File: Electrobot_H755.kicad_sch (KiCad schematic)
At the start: 108 parts, among them J1 Conn_XT30M, J10 Conn_01x04, J11 Conn_01x04, J12 Conn_01x04, J13 Conn_01x04, J14 Conn_01x04, J15 Conn_01x03, J16 Conn_01x03, J17 Conn_01x04, J18 Conn_01x03, J19 Conn_01x03, J2 Conn_01x04, J20 Conn_01x03, J21 Conn_01x03, J22 Conn_01x04, J23 Conn_01x03, J24 Conn_01x03, J25 Conn_01x03, J26 Conn_01x03, J27 Conn_01x02, J28 Conn_01x02, J29 Conn_01x02, J3 Conn_01x04, J30 Conn_01x02, J31 Conn_01x03, J32 Conn_01x03, J33 Conn_01x06, J34 Conn_01x06, J35 Conn_01x04, J36 Conn_01x02, J37 Conn_01x04, J4 Conn_01x04, J5 Conn_01x04, J6 Conn_01x04, J7 Conn_01x04, J8 Conn_01x04, J9 Conn_01x04, U2 TSR_2-2450, U3 TSR_2-2465, U4 TSR_2-2465

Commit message: Ajout des références pour les supports sécables femelle 2.54
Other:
- note added: "Support 2.54 sécable femelle à souder RS: 766-6666 / 488-1724 / 827-7659"
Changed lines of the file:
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@@
+		)
+	)
+	(text "Support 2.54 sécable femelle à souder\nRS: 766-6666 / 488-1724 / 827-7659"
+		(exclude_from_sim no)
+		(at 104.902 193.548 0)
+		(effects
+			(font
+				(size 1.016 1.016)
+			)
+			(justify left)
 		)
 	)

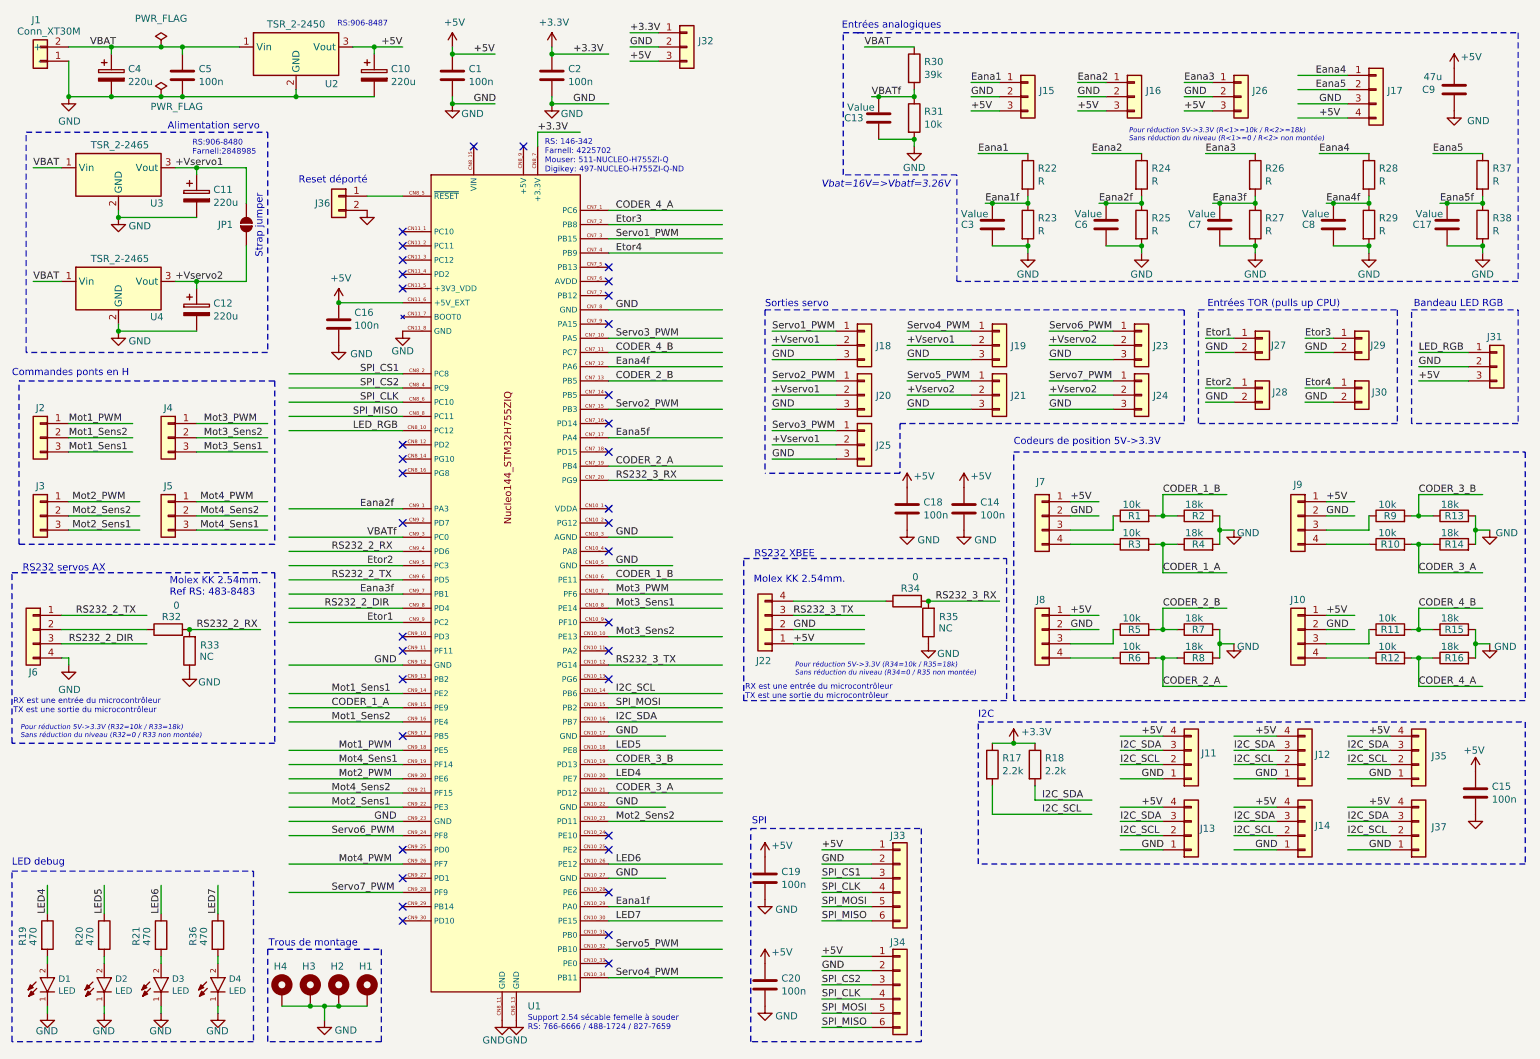
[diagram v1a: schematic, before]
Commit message: Ajout des références et valeurs manquantes sur le schéma
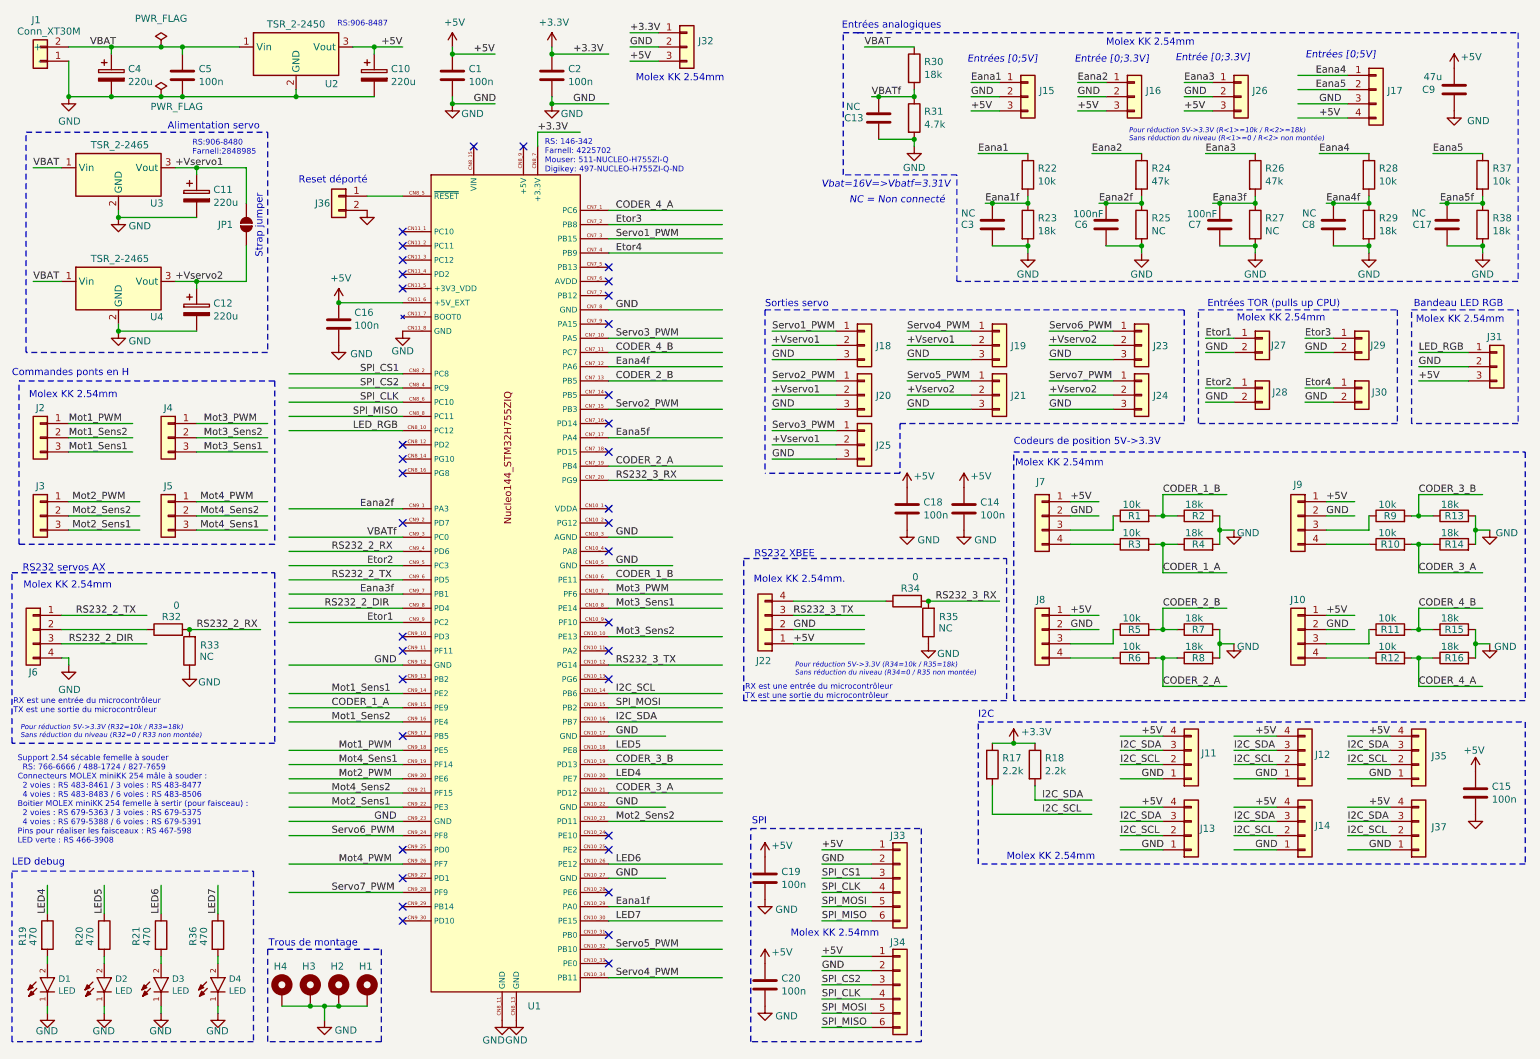
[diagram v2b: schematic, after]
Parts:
- C13, C17, C3, C8: value Value -> NC
- C6, C7: value Value -> 100nF
- R22, R28, R37: value R -> 10k
- R23, R29, R38: value R -> 18k
- R24, R26: value R -> 47k
- R25, R27: value R -> NC
- R30: value 39k -> 18k
- R31: value 10k -> 4.7k
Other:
- note added: "Entrée [0;3.3V]"
- note added: "Entrées [0;5V]"
- note added: "Molex KK 2.54mm"
- note added: "NC = Non connecté"
- note added: "Support 2.54 sécable femelle à souder RS: 766-6666 / 488-1724 / 827-7659 Connecteurs MOLEX miniKK 254 mâle à souder : 2 voies : RS 483-8461 / 3 voies : RS 483-8477 4 voies : RS 483-8483 / 6 voies : RS 483-8506 Boitier MOLEX miniKK 254 femelle à sertir (pour faisceau) : 2 voies : RS 679-5363 / 3 voies : RS 679-5375 4 voies : RS 679-5388 / 6 voies : RS 679-5391 Pins pour réaliser les faisceaux : RS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"
- note added: "Vbat=16V=>Vbatf=3.31V"
- note removed: "Molex KK 2.54mm. Ref RS: 483-8483"
- note removed: "Support 2.54 sécable femelle à souder RS: 766-6666 / 488-1724 / 827-7659"
- note removed: "Vbat=16V=>Vbatf=3.26V"
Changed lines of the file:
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@@
 		)
 	)
+	(text "Entrée [0;3.3V]"
+		(exclude_from_sim no)
+		(at 227.33 21.082 0)
+		(effects
+			(font
+				(size 1.27 1.27)
+				(italic yes)
+			)
+		)
+	)
 	(text "Sorties servo"
 		(exclude_from_sim no)
@@
 		)
 	)
-	(text "Vbat=16V=>Vbatf=3.26V"
+	(text "Molex KK 2.54mm"
+		(exclude_from_sim no)
+		(at 192.024 94.234 0)
+		(effects
+			(font
+				(size 1.27 1.27)
+			)
+			(justify left bottom)
+		)
+	)
+	(text "Molex KK 2.54mm"
+		(exclude_from_sim no)
+		(at 190.5 164.592 0)
+		(effects
+			(font
+				(size 1.27 1.27)
+			)
+			(justify left bottom)
+		)
+	)
+	(text "Entrées [0;5V]"
+		(exclude_from_sim no)
+		(at 189.738 21.336 0)
+		(effects
+			(font
+				(size 1.27 1.27)
+				(italic yes)
+			)
+		)
+	)
+	(text "Molex KK 2.54mm"
+		(exclude_from_sim no)
+		(at 124.206 25.4 0)
+		(effects
+			(font
+				(size 1.27 1.27)
+			)
+			(justify left bottom)
+		)
+	)
+	(text "Vbat=16V=>Vbatf=3.31V"
 		(exclude_from_sim no)
 		(at 168.91 43.688 0)
@@
 		)
 	)
+	(text "Molex KK 2.54mm"
+		(exclude_from_sim no)
+		(at 263.652 68.58 0)
+		(effects
+			(font
+				(size 1.27 1.27)
+			)
+			(justify left bottom)
+		)
+	)
 	(text "Commandes ponts en H"
 		(exclude_from_sim no)
@@
 		)
 	)
+	(text "Entrées [0;5V]"
+		(exclude_from_sim no)
+		(at 250.19 20.574 0)
+		(effects
+			(font
+				(size 1.27 1.27)
+				(italic yes)
+			)
+		)
+	)
 	(text "RS232 XBEE"
 		(exclude_from_sim no)
@@
 		)
 	)
-	(text "Molex KK 2.54mm.\nRef RS: 483-8483"
+	(text "Molex KK 2.54mm"
 		(exclude_from_sim no)
-		(at 40.894 117.348 0)
+		(at 14.732 116.078 0)
 		(effects
 			(font
@@
 		)
 	)
+	(text "NC = Non connecté"
+		(exclude_from_sim no)
+		(at 170.942 46.482 0)
+		(effects
+			(font
+				(size 1.27 1.27)
+				(italic yes)
+			)
+		)
+	)
 	(text "Pour réduction 5V->3.3V (R32=10k / R33=18k)\nSans réduction du niveau (R32=0 / R33 non montée)\n\n"
 		(exclude_from_sim no)
@@
 		)
 	)
+	(text "Entrée [0;3.3V]"
+		(exclude_from_sim no)
+		(at 209.296 21.336 0)
+		(effects
+			(font
+				(size 1.27 1.27)
+				(italic yes)
+			)
+		)
+	)
 	(text "Entrées TOR (pulls up CPU)"
 		(exclude_from_sim no)
@@
 		)
 	)
-	(text "Support 2.54 sécable femelle à souder\nRS: 766-6666 / 488-1724 / 827-7659"
+	(text "Molex KK 2.54mm"
 		(exclude_from_sim no)
-		(at 104.902 193.548 0)
+		(at 231.648 68.326 0)
 		(effects
 			(font
-				(size 1.016 1.016)
+				(size 1.27 1.27)
 			)
-			(justify left)
+			(justify left bottom)
 		)
 	)
@@
 		)
 	)
+	(text "Molex KK 2.54mm"
+		(exclude_from_sim no)
+		(at 151.892 178.308 0)
+		(effects
+			(font
+				(size 1.27 1.27)
+			)
+			(justify left bottom)
+		)
+	)
 	(text "RS232 servos AX"
 		(exclude_from_sim no)
@@
 		)
 	)
+	(text "Molex KK 2.54mm"
+		(exclude_from_sim no)
+		(at 208.28 19.05 0)
+		(effects
+			(font
+				(size 1.27 1.27)
+			)
+			(justify left bottom)
+		)
+	)
 	(text "I2C"
 		(exclude_from_sim no)
@@
 		)
 	)
+	(text "Molex KK 2.54mm"
+		(exclude_from_sim no)
+		(at 15.748 82.042 0)
+		(effects
+			(font
+				(size 1.27 1.27)
+			)
+			(justify left bottom)
+		)
+	)
 	(text "Entrées analogiques"
 		(exclude_from_sim no)
@@
 		)
 	)
+	(text "Support 2.54 sécable femelle à souder\n  RS: 766-6666 / 488-1724 / 827-7659\nConnecteurs MOLEX miniKK 254 mâle à souder :\n  2 voies : RS 483-8461 / 3 voies : RS 483-8477\n  4 voies : RS 483-8483 / 6 voies : RS 483-8506\nBoitier MOLEX miniKK 254 femelle à sertir (pour faisceau) : \n  2 voies : RS 679-5363 / 3 voies : RS 679-5375\n  4 voies : RS 679-5388 / 6 voies : RS 679-5391\nPins pour réaliser les faisceaux : RS 467-598\nLED verte : RS 466-3908"
+		(exclude_from_sim no)
+		(at 13.716 153.67 0)
+		(effects
+			(font
+				(size 1.016 1.016)
+				(color 255 123 22 1)
+			)
+			(justify left)
+		)
+	)
 	(text "Strap jumper"
 		(exclude_from_sim no)
@@
 			)
 		)
-		(property "Value" "Value"
-			(at 184.785 48.895 0)
+		(property "Value" "NC"
+			(at 183.642 48.768 0)
 			(effects
 				(font
@@
 			)
 		)
-		(property "Value" "R"
+		(property "Value" "18k"
 			(at 277.368 51.943 0)
 			(effects
@@
 			)
 		)
-		(property "Value" "10k"
+		(property "Value" "4.7k"
 			(at 175.768 32.893 0)
 			(effects
@@
 			)
 		)
-		(property "Value" "Value"
+		(property "Value" "100nF"
 			(at 205.105 48.895 0)
 			(effects
@@
 			)
 		)
-		(property "Value" "R"
+		(property "Value" "18k"
 			(at 196.088 51.943 0)
 			(effects
@@
 			)
 		)
-		(property "Value" "Value"
-			(at 266.065 48.895 0)
+		(property "Value" "NC"
+			(at 264.16 48.768 0)
 			(effects
 				(font
@@
 			)
 		)
-		(property "Value" "R"
+		(property "Value" "NC"
 			(at 236.728 51.943 0)
 			(effects
@@
 			)
 		)
-		(property "Value" "R"
+		(property "Value" "10k"
 			(at 196.088 43.053 0)
 			(effects
@@
 			)
 		)
-		(property "Value" "R"
+		(property "Value" "18k"
 			(at 257.048 51.943 0)
 			(effects
@@
 			)
 		)
-		(property "Value" "R"
+		(property "Value" "10k"
 			(at 257.048 43.053 0)
 			(effects
@@
 			)
 		)
-		(property "Value" "R"
+		(property "Value" "47k"
 			(at 236.728 43.053 0)
 			(effects
@@
 			)
 		)
-		(property "Value" "39k"
+		(property "Value" "18k"
 			(at 175.768 24.003 0)
 			(effects
@@
 			)
 		)
-		(property "Value" "R"
+		(property "Value" "NC"
 			(at 216.408 51.943 0)
 			(effects
@@
 			)
 		)
-		(property "Value" "Value"
+		(property "Value" "100nF"
 			(at 225.425 48.895 0)
 			(effects
@@
 			)
 		)
-		(property "Value" "R"
+		(property "Value" "47k"
 			(at 216.408 43.053 0)
 			(effects
@@
 			)
 		)
-		(property "Value" "Value"
-			(at 164.465 29.845 0)
+		(property "Value" "NC"
+			(at 163.068 29.718 0)
 			(effects
 				(font
@@
 			)
 		)
-		(property "Value" "Value"
-			(at 245.745 48.895 0)
+		(property "Value" "NC"
+			(at 244.602 48.768 0)
 			(effects
 				(font
@@
 			)
 		)
-		(property "Value" "R"
+		(property "Value" "10k"
 			(at 277.368 43.053 0)
 			(effects
